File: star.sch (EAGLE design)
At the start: 32 parts, among them J1 M03X2-NOSILK, J2 CON_TERMINAL_HOLES, U2 V_REG_MCP170X-CB

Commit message: It's a star, not a snowflake.
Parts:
- U2: value V_REG_MCP170X-CB -> V_REG_MCP170X-CB-NOSILK; device adi-misc:V_REG_MCP170X-CB -> snowflake:V_REG_MCP170X-CB-NOSILK
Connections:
- net GND: now also J2.2; no longer J2.1
- net N$1: now also J2.1; no longer J2.2
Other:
- moved on the sheet: J2
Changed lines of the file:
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@@
 <part name="SUPPLY2" library="SparkFun-Aesthetics" deviceset="VCC" device=""/>
 <part name="GND5" library="SparkFun-Aesthetics" deviceset="GND" device=""/>
-<part name="U2" library="adi-misc" deviceset="V_REG_MCP170X" device="-CB"/>
+<part name="U2" library="snowflake" deviceset="V_REG_MCP170X" device="-CB-NOSILK"/>
 <part name="J2" library="adi-misc" deviceset="CON_TERMINAL_HOLES" device=""/>
 </parts>
@@
 <instance part="GND5" gate="1" x="20.32" y="71.12"/>
 <instance part="U2" gate="G$1" x="40.64" y="83.82"/>
-<instance part="J2" gate="G$1" x="17.78" y="81.28" rot="R180"/>
+<instance part="J2" gate="G$1" x="17.78" y="83.82" rot="MR0"/>
 </instances>
 <busses>
@@
 <pinref part="GND5" gate="1" pin="GND"/>
 <wire x1="20.32" y1="81.28" x2="20.32" y2="73.66" width="0.1524" layer="91"/>
-<pinref part="J2" gate="G$1" pin="1"/>
+<pinref part="J2" gate="G$1" pin="2"/>
 <wire x1="17.78" y1="81.28" x2="20.32" y2="81.28" width="0.1524" layer="91"/>
 </segment>
@@
 <pinref part="U2" gate="G$1" pin="IN"/>
 <wire x1="27.94" y1="83.82" x2="33.02" y2="83.82" width="0.1524" layer="91"/>
-<pinref part="J2" gate="G$1" pin="2"/>
+<pinref part="J2" gate="G$1" pin="1"/>
 <wire x1="17.78" y1="83.82" x2="27.94" y2="83.82" width="0.1524" layer="91"/>
 <junction x="27.94" y="83.82"/>

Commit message: Removed redundant cap.
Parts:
- removed C3: (no value), snowflake:C_0805NOSILK
- J1: value M03X2-NOSILK -> CON_TERMINAL_HOLES; device snowflake:M03X2-NOSILK -> adi-misc:CON_TERMINAL_HOLES
- J2: value CON_TERMINAL_HOLES -> M03X2-NOSILK; device adi-misc:CON_TERMINAL_HOLES -> snowflake:M03X2-NOSILK
- U1: value (none) -> V_REG_MCP170X-CB-NOSILK; device snowflake:ATTINY5-20SU-NOSILK -> snowflake:V_REG_MCP170X-CB-NOSILK
- U2: value V_REG_MCP170X-CB-NOSILK -> (none); device snowflake:V_REG_MCP170X-CB-NOSILK -> snowflake:ATTINY5-20SU-NOSILK
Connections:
- net GND: now also J1.2, J2.6; no longer C3.1, J1.6, J2.2
- net MISO: now also J2.1, U2.PB1(MISO/DO/AIN1/OC0B/OC1A/PCINT1); no longer J1.1, U1.PB1(MISO/DO/AIN1/OC0B/OC1A/PCINT1)
- net MOSI: now also J2.4, U2.PB0(MOSI/DI/SDA/AIN0/OC0A/OC1A/AREF/PCINT0); no longer J1.4, U1.PB0(MOSI/DI/SDA/AIN0/OC0A/OC1A/AREF/PCINT0)
- net N$1: now also C1.2, J1.1, U1.IN; no longer C2.2, J2.1, U2.IN
- net N$4: now also U2.PB3(PCINT3/XTAL1/CLKI/OC1B/ADC3); no longer U1.PB3(PCINT3/XTAL1/CLKI/OC1B/ADC3)
- net N$5: now also U2.PB4(PCINT4/XTAL2/CLKO/OC1B/ADC2); no longer U1.PB4(PCINT4/XTAL2/CLKO/OC1B/ADC2)
- net RST: now also J2.5, U2.PB5(PCINT5/RESET/ADC0/DW); no longer J1.5, U1.PB5(PCINT5/RESET/ADC0/DW)
- net SCK: now also J2.3, U2.PB2(SCK/USCK/SCL/ADC1/T0/INT0/PCINT2); no longer J1.3, U1.PB2(SCK/USCK/SCL/ADC1/T0/INT0/PCINT2)
- net VCC: now also C2.2, J2.2, U1.OUT, U2.VCC; no longer C1.2, C3.2, J1.2, U1.VCC, U2.OUT
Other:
- moved on the sheet: C1, C2

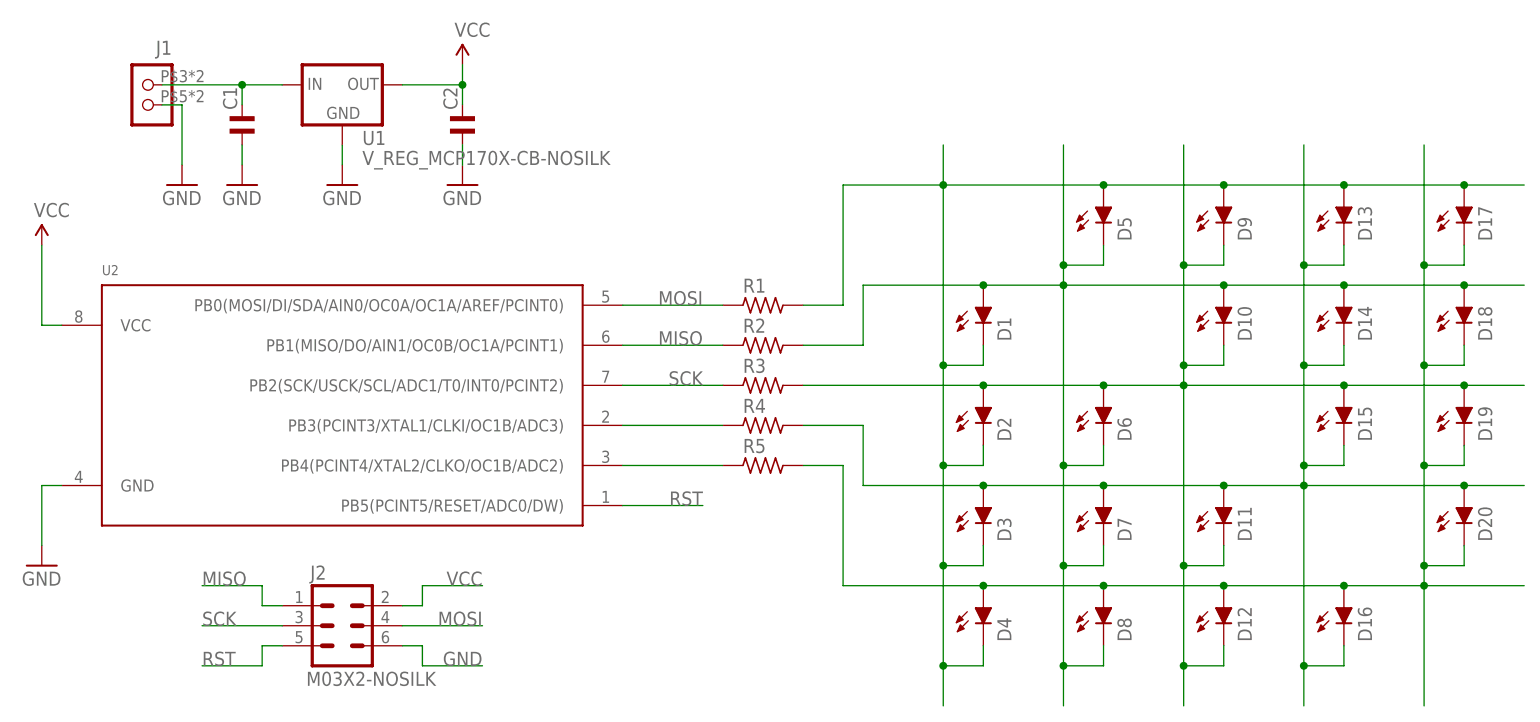
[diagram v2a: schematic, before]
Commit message: Created png. Added values to schematic.
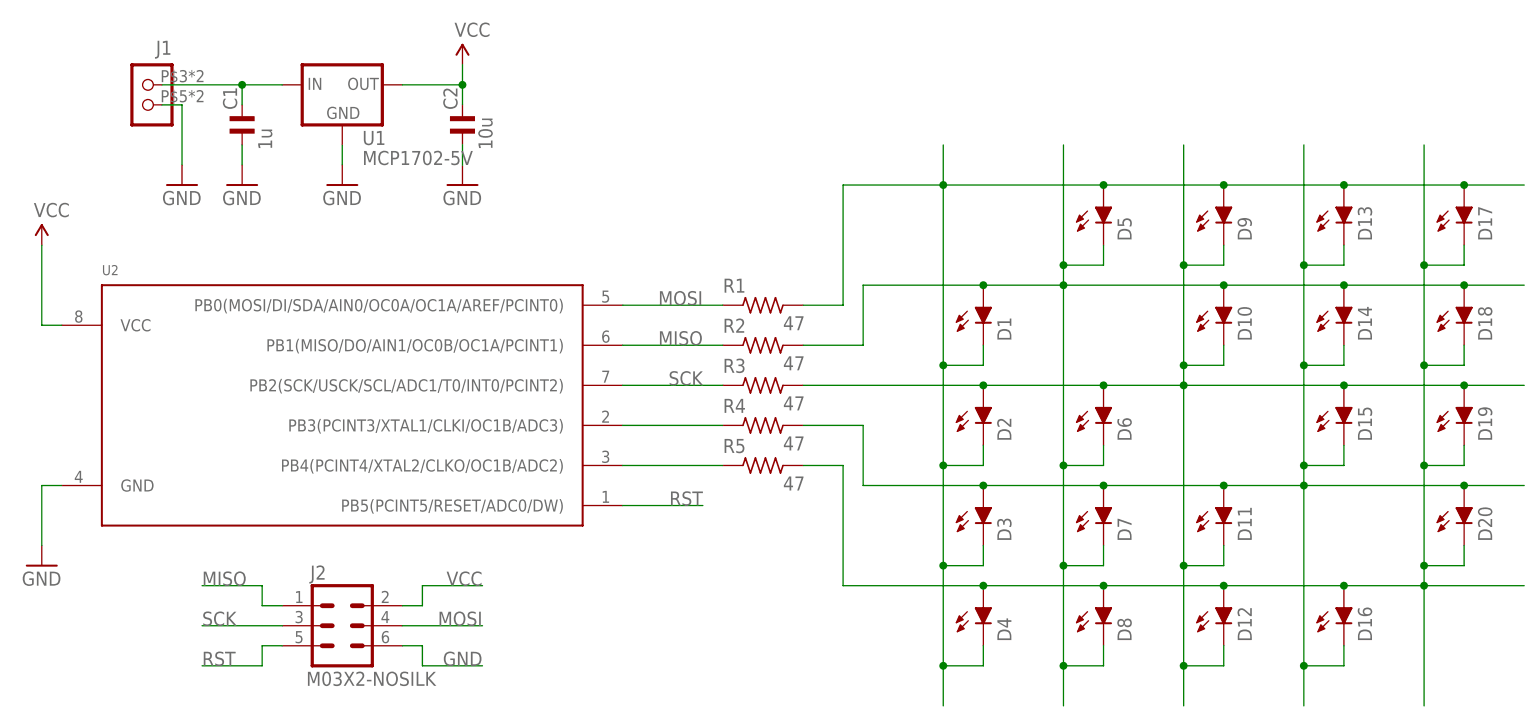
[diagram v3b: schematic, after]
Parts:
- C1: value (none) -> 1u
- C2: value (none) -> 10u
- R1, R2, R3, R4, R5: value (none) -> 47
- U1: value V_REG_MCP170X-CB-NOSILK -> MCP1702-5V
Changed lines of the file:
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@@
 <layer number="91" name="Nets" color="2" fill="1" visible="yes" active="yes"/>
 <layer number="92" name="Busses" color="1" fill="1" visible="yes" active="yes"/>
-<layer number="93" name="Pins" color="2" fill="1" visible="yes" active="yes"/>
+<layer number="93" name="Pins" color="2" fill="1" visible="no" active="yes"/>
 <layer number="94" name="Symbols" color="4" fill="1" visible="yes" active="yes"/>
 <layer number="95" name="Names" color="7" fill="1" visible="yes" active="yes"/>
@@
 <parts>
 <part name="U2" library="snowflake" deviceset="ATTINY*5" device="-20SU-NOSILK"/>
-<part name="R1" library="snowflake" deviceset="R_" device="0805NOSILK"/>
-<part name="R2" library="snowflake" deviceset="R_" device="0805NOSILK"/>
-<part name="R3" library="snowflake" deviceset="R_" device="0805NOSILK"/>
-<part name="R4" library="snowflake" deviceset="R_" device="0805NOSILK"/>
-<part name="R5" library="snowflake" deviceset="R_" device="0805NOSILK"/>
+<part name="R1" library="snowflake" deviceset="R_" device="0805NOSILK" value="47"/>
+<part name="R2" library="snowflake" deviceset="R_" device="0805NOSILK" value="47"/>
+<part name="R3" library="snowflake" deviceset="R_" device="0805NOSILK" value="47"/>
+<part name="R4" library="snowflake" deviceset="R_" device="0805NOSILK" value="47"/>
+<part name="R5" library="snowflake" deviceset="R_" device="0805NOSILK" value="47"/>
 <part name="SUPPLY1" library="SparkFun-Aesthetics" deviceset="VCC" device=""/>
 <part name="GND1" library="SparkFun-Aesthetics" deviceset="GND" device=""/>
@@
 <part name="D20" library="snowflake" deviceset="LED" device="CHIP-LED0805NOSILK"/>
 <part name="J2" library="snowflake" deviceset="M03X2" device="-NOSILK"/>
-<part name="C1" library="snowflake" deviceset="C_" device="0805NOSILK"/>
-<part name="C2" library="snowflake" deviceset="C_" device="0805NOSILK"/>
+<part name="C1" library="snowflake" deviceset="C_" device="0805NOSILK" value="1u"/>
+<part name="C2" library="snowflake" deviceset="C_" device="0805NOSILK" value="10u"/>
 <part name="GND3" library="SparkFun-Aesthetics" deviceset="GND" device=""/>
 <part name="GND4" library="SparkFun-Aesthetics" deviceset="GND" device=""/>
@@
 <part name="SUPPLY2" library="SparkFun-Aesthetics" deviceset="VCC" device=""/>
 <part name="GND2" library="SparkFun-Aesthetics" deviceset="GND" device=""/>
-<part name="U1" library="snowflake" deviceset="V_REG_MCP170X" device="-CB-NOSILK"/>
+<part name="U1" library="snowflake" deviceset="V_REG_MCP170X" device="-CB-NOSILK" value="MCP1702-5V"/>
 <part name="J1" library="adi-misc" deviceset="CON_TERMINAL_HOLES" device=""/>
 </parts>
@@
 <instances>
 <instance part="U2" gate="G$1" x="40.64" y="43.18"/>
-<instance part="R1" gate="G$1" x="93.98" y="55.88"/>
-<instance part="R2" gate="G$1" x="93.98" y="50.8"/>
-<instance part="R3" gate="G$1" x="93.98" y="45.72"/>
-<instance part="R4" gate="G$1" x="93.98" y="40.64"/>
-<instance part="R5" gate="G$1" x="93.98" y="35.56"/>
+<instance part="R1" gate="G$1" x="93.98" y="55.88" smashed="yes">
+<attribute name="NAME" x="88.9" y="57.4675" size="1.778" layer="95"/>
+<attribute name="VALUE" x="96.52" y="52.705" size="1.778" layer="96"/>
+</instance>
+<instance part="R2" gate="G$1" x="93.98" y="50.8" smashed="yes">
+<attribute name="NAME" x="88.9" y="52.3875" size="1.778" layer="95"/>
+<attribute name="VALUE" x="96.52" y="47.625" size="1.778" layer="96"/>
+</instance>
+<instance part="R3" gate="G$1" x="93.98" y="45.72" smashed="yes">
+<attribute name="NAME" x="88.9" y="47.3075" size="1.778" layer="95"/>
+<attribute name="VALUE" x="96.52" y="42.545" size="1.778" layer="96"/>
+</instance>
+<instance part="R4" gate="G$1" x="93.98" y="40.64" smashed="yes">
+<attribute name="NAME" x="88.9" y="42.2275" size="1.778" layer="95"/>
+<attribute name="VALUE" x="96.52" y="37.465" size="1.778" layer="96"/>
+</instance>
+<instance part="R5" gate="G$1" x="93.98" y="35.56" smashed="yes">
+<attribute name="NAME" x="88.9" y="37.1475" size="1.778" layer="95"/>
+<attribute name="VALUE" x="96.52" y="32.385" size="1.778" layer="96"/>
+</instance>
 <instance part="SUPPLY1" gate="G$1" x="2.54" y="63.5"/>
 <instance part="GND1" gate="1" x="2.54" y="22.86"/>
